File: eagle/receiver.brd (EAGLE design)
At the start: 75.9 x 63.5 mm, 18 parts, among them IC1 7805TV, Q1 16 Mhz, U1 ATMEGA328P-PU

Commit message: Fixed reversed DC power jack and finished PCB
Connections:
- removed net N$8: 9V-JACK.RING, JP5.2
- new net N$7: 9V-JACK.TIP, JP5.2
- net GND: now also 9V-JACK.RING; no longer 9V-JACK.TIP
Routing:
- net GND: track 279.7 -> 302.3 mm
- net N$1: track 47.5 -> 28.4 mm
- net N$7: track 0.00 -> 13.6 mm
- net N$8: track 11.5 -> 0.00 mm
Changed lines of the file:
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@@
 <contactref element="U1" pad="22"/>
 <contactref element="U1" pad="8"/>
-<contactref element="9V-JACK" pad="TIP"/>
 <contactref element="PNA4601M" pad="2"/>
 <contactref element="S1" pad="3"/>
 <contactref element="S1" pad="4"/>
-<wire x1="22.9616" y1="20.32" x2="22.9616" y2="16.6624" width="0.6096" layer="16"/>
-<wire x1="22.9616" y1="16.6624" x2="22.9616" y2="12.8016" width="0.6096" layer="16"/>
+<wire x1="22.9616" y1="20.32" x2="22.9616" y2="18.415" width="0.6096" layer="16"/>
+<wire x1="22.9616" y1="18.415" x2="22.9616" y2="12.8016" width="0.6096" layer="16"/>
 <wire x1="22.9616" y1="12.8016" x2="22.86" y2="12.7" width="0.6096" layer="16"/>
 <wire x1="22.9616" y1="20.32" x2="22.86" y2="20.32" width="0.6096" layer="16"/>
-<wire x1="7.7216" y1="30.6832" x2="7.7216" y2="35.56" width="0.6096" layer="16"/>
-<wire x1="10.3632" y1="28.0416" x2="7.7216" y2="30.6832" width="0.6096" layer="16"/>
-<wire x1="10.3632" y1="16.6624" x2="10.3632" y2="28.0416" width="0.6096" layer="16"/>
 <wire x1="7.7216" y1="35.56" x2="7.62" y2="35.56" width="0.6096" layer="16"/>
-<wire x1="10.3632" y1="16.6624" x2="10.56" y2="16.61" width="0.6096" layer="16"/>
-<wire x1="10.7696" y1="16.6624" x2="22.9616" y2="16.6624" width="0.6096" layer="16"/>
-<wire x1="10.7696" y1="16.6624" x2="10.56" y2="16.61" width="0.6096" layer="16"/>
 <wire x1="26.8224" y1="58.3184" x2="26.8224" y2="53.4416" width="0.6096" layer="16"/>
 <wire x1="26.8224" y1="53.4416" x2="26.67" y2="53.34" width="0.6096" layer="16"/>
@@
 <wire x1="47.1424" y1="59.5376" x2="46.99" y2="59.69" width="0.6096" layer="16"/>
 <wire x1="47.3456" y1="43.2816" x2="46.99" y2="43.18" width="0.6096" layer="16"/>
-<wire x1="7.5184" y1="45.72" x2="7.5184" y2="35.7632" width="0.6096" layer="16"/>
+<wire x1="7.5184" y1="45.72" x2="7.5184" y2="41.275" width="0.6096" layer="16"/>
+<wire x1="7.5184" y1="41.275" x2="7.5184" y2="35.7632" width="0.6096" layer="16"/>
 <wire x1="3.6576" y1="49.5808" x2="7.5184" y2="45.72" width="0.6096" layer="16"/>
 <wire x1="3.6576" y1="58.1152" x2="3.6576" y2="49.5808" width="0.6096" layer="16"/>
@@
 <wire x1="48.3616" y1="24.1808" x2="48.26" y2="24.13" width="0.6096" layer="16"/>
 <wire x1="48.1584" y1="24.1808" x2="48.26" y2="24.13" width="0.6096" layer="16"/>
+<contactref element="9V-JACK" pad="RING"/>
+<wire x1="15.24" y1="18.415" x2="22.9616" y2="18.415" width="0.6096" layer="16"/>
+<wire x1="15.24" y1="27.305" x2="15.24" y2="18.415" width="0.6096" layer="16"/>
+<wire x1="7.62" y1="34.925" x2="15.24" y2="27.305" width="0.6096" layer="16"/>
+<wire x1="7.62" y1="35.56" x2="7.62" y2="34.925" width="0.6096" layer="16"/>
+<wire x1="3.175" y1="18.415" x2="4.445" y2="17.145" width="0.6096" layer="16"/>
+<wire x1="3.175" y1="36.83" x2="3.175" y2="18.415" width="0.6096" layer="16"/>
+<wire x1="7.62" y1="41.275" x2="3.175" y2="36.83" width="0.6096" layer="16"/>
+<wire x1="4.445" y1="17.145" x2="4.66" y2="16.61" width="0.6096" layer="16"/>
+<wire x1="7.62" y1="41.275" x2="7.5184" y2="41.275" width="0.6096" layer="16"/>
 </signal>
 <signal name="N$1" class="1">
@@
 <contactref element="C1" pad="+"/>
 <contactref element="JP5" pad="1"/>
-<wire x1="12.8016" y1="12.5984" x2="17.6784" y2="12.5984" width="0.6096" layer="16"/>
-<wire x1="8.9408" y1="8.7376" x2="12.8016" y2="12.5984" width="0.6096" layer="16"/>
-<wire x1="6.2992" y1="8.7376" x2="8.9408" y2="8.7376" width="0.6096" layer="16"/>
-<wire x1="1.4224" y1="13.6144" x2="6.2992" y2="8.7376" width="0.6096" layer="16"/>
-<wire x1="1.4224" y1="27.0256" x2="1.4224" y2="13.6144" width="0.6096" layer="16"/>
-<wire x1="4.4704" y1="30.0736" x2="1.4224" y2="27.0256" width="0.6096" layer="16"/>
-<wire x1="5.6896" y1="30.0736" x2="5.08" y2="30.0736" width="0.6096" layer="16"/>
-<wire x1="5.08" y1="30.0736" x2="4.4704" y2="30.0736" width="0.6096" layer="16"/>
-<wire x1="7.7216" y1="28.0416" x2="5.6896" y2="30.0736" width="0.6096" layer="16"/>
 <wire x1="17.6784" y1="12.5984" x2="17.78" y2="12.7" width="0.6096" layer="16"/>
 <wire x1="7.7216" y1="28.0416" x2="7.62" y2="27.94" width="0.6096" layer="16"/>
-<wire x1="5.08" y1="30.0736" x2="5.08" y2="35.56" width="0.6096" layer="16"/>
+<wire x1="13.97" y1="16.51" x2="17.78" y2="12.7" width="0.6096" layer="16"/>
+<wire x1="13.97" y1="21.59" x2="13.97" y2="16.51" width="0.6096" layer="16"/>
+<wire x1="7.62" y1="27.94" x2="13.97" y2="21.59" width="0.6096" layer="16"/>
+<wire x1="5.715" y1="34.925" x2="5.08" y2="35.56" width="0.6096" layer="16"/>
+<wire x1="5.715" y1="30.48" x2="5.715" y2="34.925" width="0.6096" layer="16"/>
+<wire x1="7.62" y1="28.575" x2="5.715" y2="30.48" width="0.6096" layer="16"/>
+<wire x1="7.62" y1="27.94" x2="7.62" y2="28.575" width="0.6096" layer="16"/>
 </signal>
 <signal name="N$2">
@@
 <signal name="S$1">
 </signal>
-<signal name="N$8" class="1">
-<contactref element="9V-JACK" pad="RING"/>
-<contactref element="JP5" pad="2"/>
-<wire x1="5.08" y1="17.0688" x2="5.08" y2="27.94" width="0.6096" layer="16"/>
-<wire x1="4.6736" y1="16.6624" x2="5.08" y2="17.0688" width="0.6096" layer="16"/>
-<wire x1="4.6736" y1="16.6624" x2="4.66" y2="16.61" width="0.6096" layer="16"/>
-</signal>
 <signal name="IR">
 <contactref element="PNA4601M" pad="1"/>
@@
 <wire x1="48.3616" y1="21.5392" x2="48.26" y2="21.59" width="0.4064" layer="16"/>
 </signal>
+<signal name="N$7" class="1">
+<contactref element="9V-JACK" pad="TIP"/>
+<contactref element="JP5" pad="2"/>
+<wire x1="5.715" y1="27.305" x2="5.08" y2="27.94" width="0.6096" layer="16"/>
+<wire x1="5.715" y1="21.59" x2="5.715" y2="27.305" width="0.6096" layer="16"/>
+<wire x1="10.16" y1="17.145" x2="5.715" y2="21.59" width="0.6096" layer="16"/>
+<wire x1="10.16" y1="17.145" x2="10.56" y2="16.61" width="0.6096" layer="16"/>
+</signal>
 </signals>

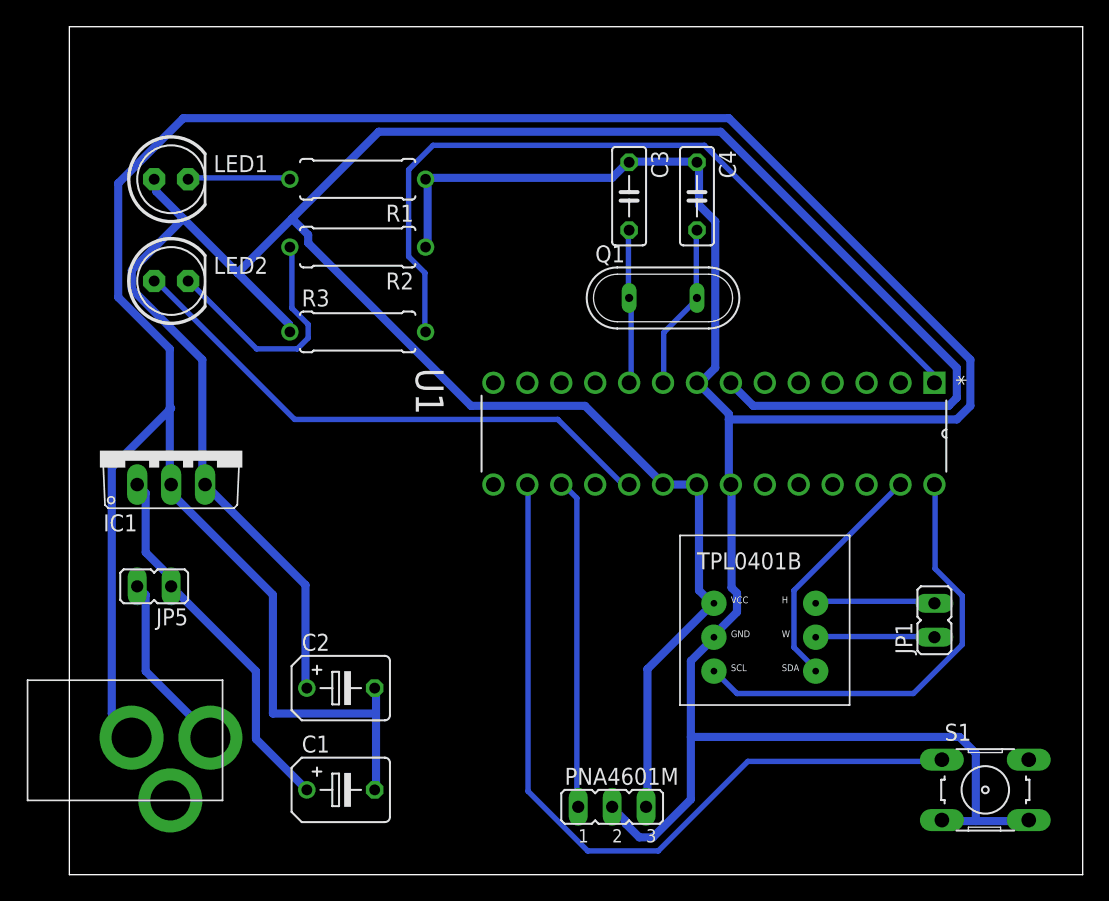
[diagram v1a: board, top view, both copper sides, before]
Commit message: Removed dpot from project and replaced with single input MUX
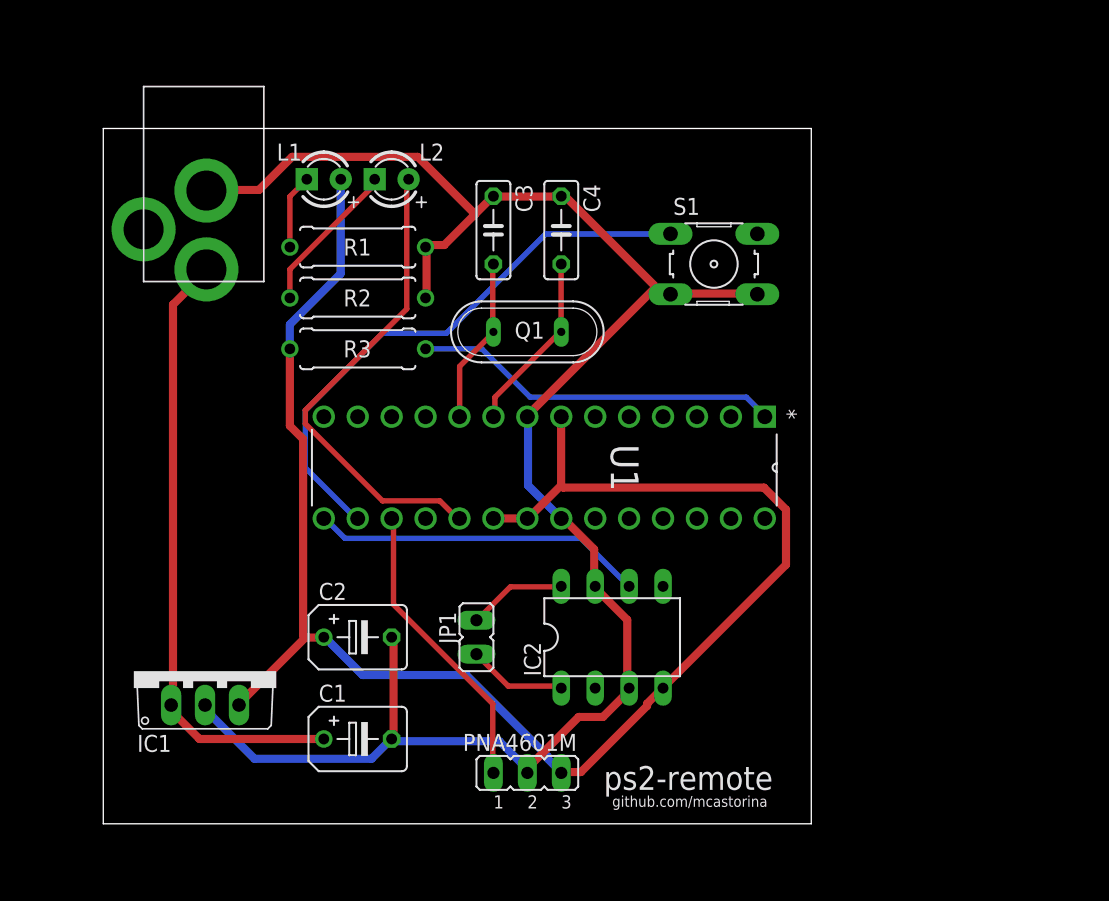
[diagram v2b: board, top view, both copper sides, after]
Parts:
- removed JP5: (no value), jumper:JP1
- removed LED1, LED2: (no value), adafruit:LED5MM
- removed U$1: TPL0401B, tpl0401b:TPL0401B
- added IC2: DG417CJ, maxim:DIL08
- added L1, L2: (no value), EE445L:LED3MM
- R1, R2: value 220 -> 330
- moved 9V-JACK 45.3 mm to (10.2, 61.0), turned to 0 degrees
- moved S1 44.3 mm to (48.3, 52.1)
- moved JP1 34.3 mm to (30.5, 24.1), turned to 180 degrees
- moved IC1 16.7 mm to (10.2, 21.6)
- moved U1 13.0 mm to (19.1, 33.0)
- moved C4 10.5 mm to (36.8, 54.6)
- moved Q1 10.5 mm to (34.3, 47.0)
- moved C3 10.5 mm to (31.8, 54.6)
- moved PNA4601M 6.84 mm to (34.3, 14.0)
- moved R1 5.08 mm to (21.6, 53.3)
- moved C1 4.02 mm to (21.6, 16.5)
- moved C2 4.02 mm to (21.6, 24.1)
- moved R2 3.81 mm to (21.6, 49.5)
- moved R3 1.27 mm to (21.6, 45.7), turned to 180 degrees
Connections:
- removed net N$1: C1.+, IC1.1, JP5.1
- removed net SCL: U$1.SCL, U1.28
- removed net SDA: U$1.SDA, U1.27
- new net SW: IC2.6, U1.15
- new net VL: IC2.5
- net 5V: now also IC2.4, L1.A, R3.2; no longer LED1.A, R3.1, U$1.VDD
- net GND: now also IC2.3, IC2.7; no longer U$1.GND
- net N$2: now also L1.K; no longer LED1.K
- net N$3: now also IC2.1, JP1.2; no longer JP1.1, U$1.W
- net N$6: now also IC2.8, JP1.1; no longer JP1.2, U$1.H
- net N$7: now also C1.+, IC1.1; no longer JP5.2
- net N$9: now also L2.K; no longer LED2.K
- net RESET: now also R3.1; no longer R3.2
- net SCK: now also L2.A; no longer LED2.A
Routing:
- net GND: track 302.3 -> 141.0 mm
- net 5V: track 209.8 -> 123.3 mm
- net SCL: track 33.7 -> 0.00 mm
- net RESET: track 60.5 -> 27.5 mm
- net N$7: track 13.6 -> 46.4 mm
- net N$1: track 28.4 -> 0.00 mm
- net SW: track 0.00 -> 25.0 mm
- net SDA: track 18.0 -> 0.00 mm
- net BTN: track 58.7 -> 42.6 mm
- net N$9: track 18.8 -> 11.5 mm
- net SCK: track 41.9 -> 36.0 mm
- net IR: track 24.7 -> 22.3 mm
- net N$2: track 7.75 -> 5.60 mm
- net N$6: track 9.11 -> 7.41 mm
- net N$3: track 8.95 -> 7.48 mm
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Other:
- board size 75.9 x 63.5 mm -> 53 x 52.1 mm
- board text added: "github.com/mcastorina"
- board text added: "ps2-remote"
